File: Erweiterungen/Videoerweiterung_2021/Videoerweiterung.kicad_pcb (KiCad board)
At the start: 2 copper layers, 141.5 x 160 mm, 145 parts, among them X200 Bus, X201 ~CS2, X202 XTAL, X203 select, X204 ~KEY, X205 BUSY, X206 POWER, X300 8k RAM-Modul, X301 8k RAM-Modul, X302 8k RAM-Modul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

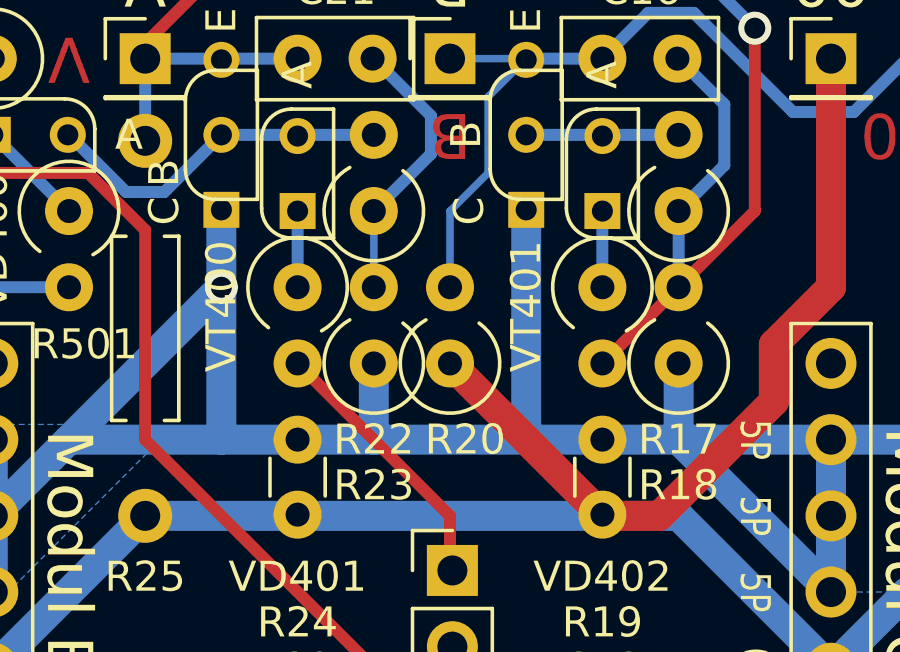
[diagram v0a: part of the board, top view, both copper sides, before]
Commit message: R20 gedreht
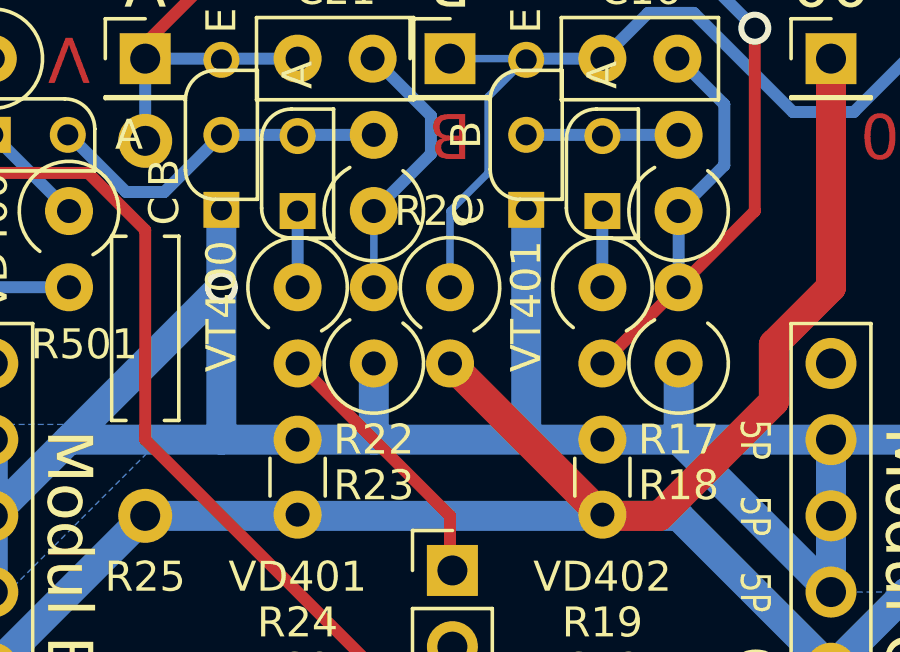
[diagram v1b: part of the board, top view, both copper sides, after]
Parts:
- D13: value UB8830 -> UB8860
- moved R20 2.54 mm to (121.9, 61.0), turned to 270 degrees
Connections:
- R20 pad 1: GND -> B
- R20 pad 2: B -> GND

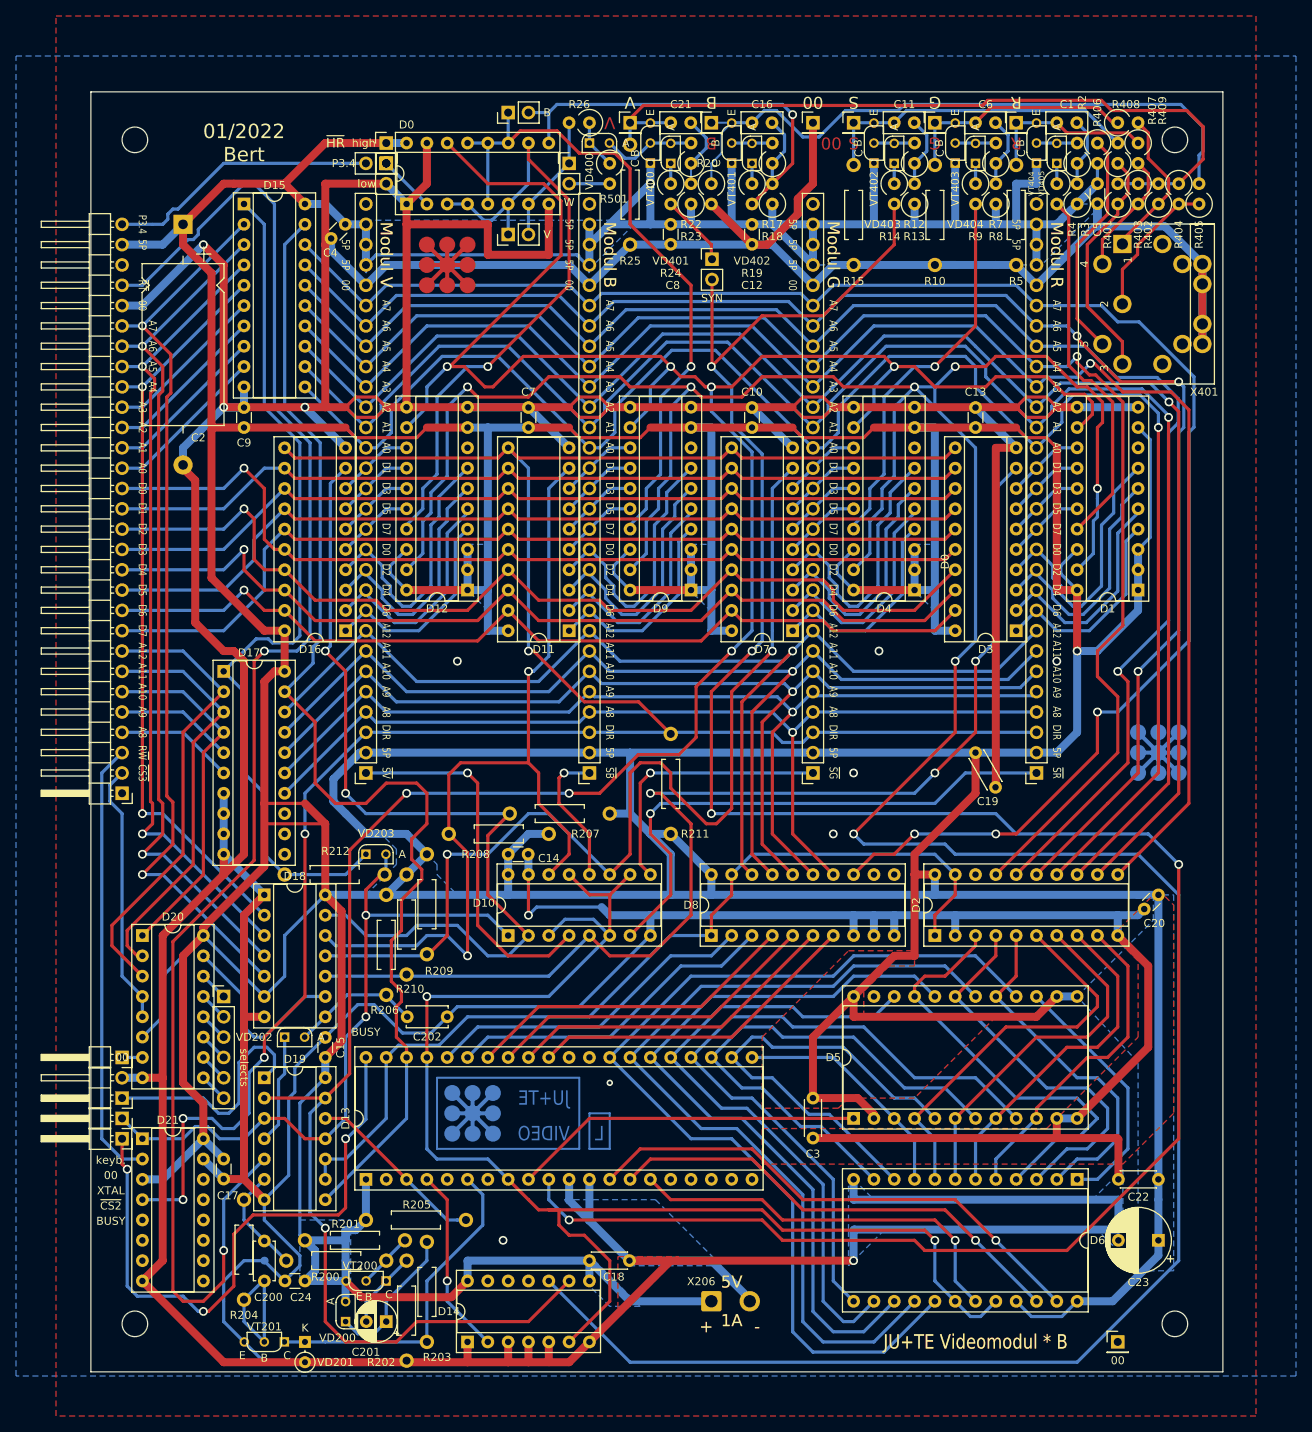
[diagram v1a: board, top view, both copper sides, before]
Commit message: PCB korrigiert
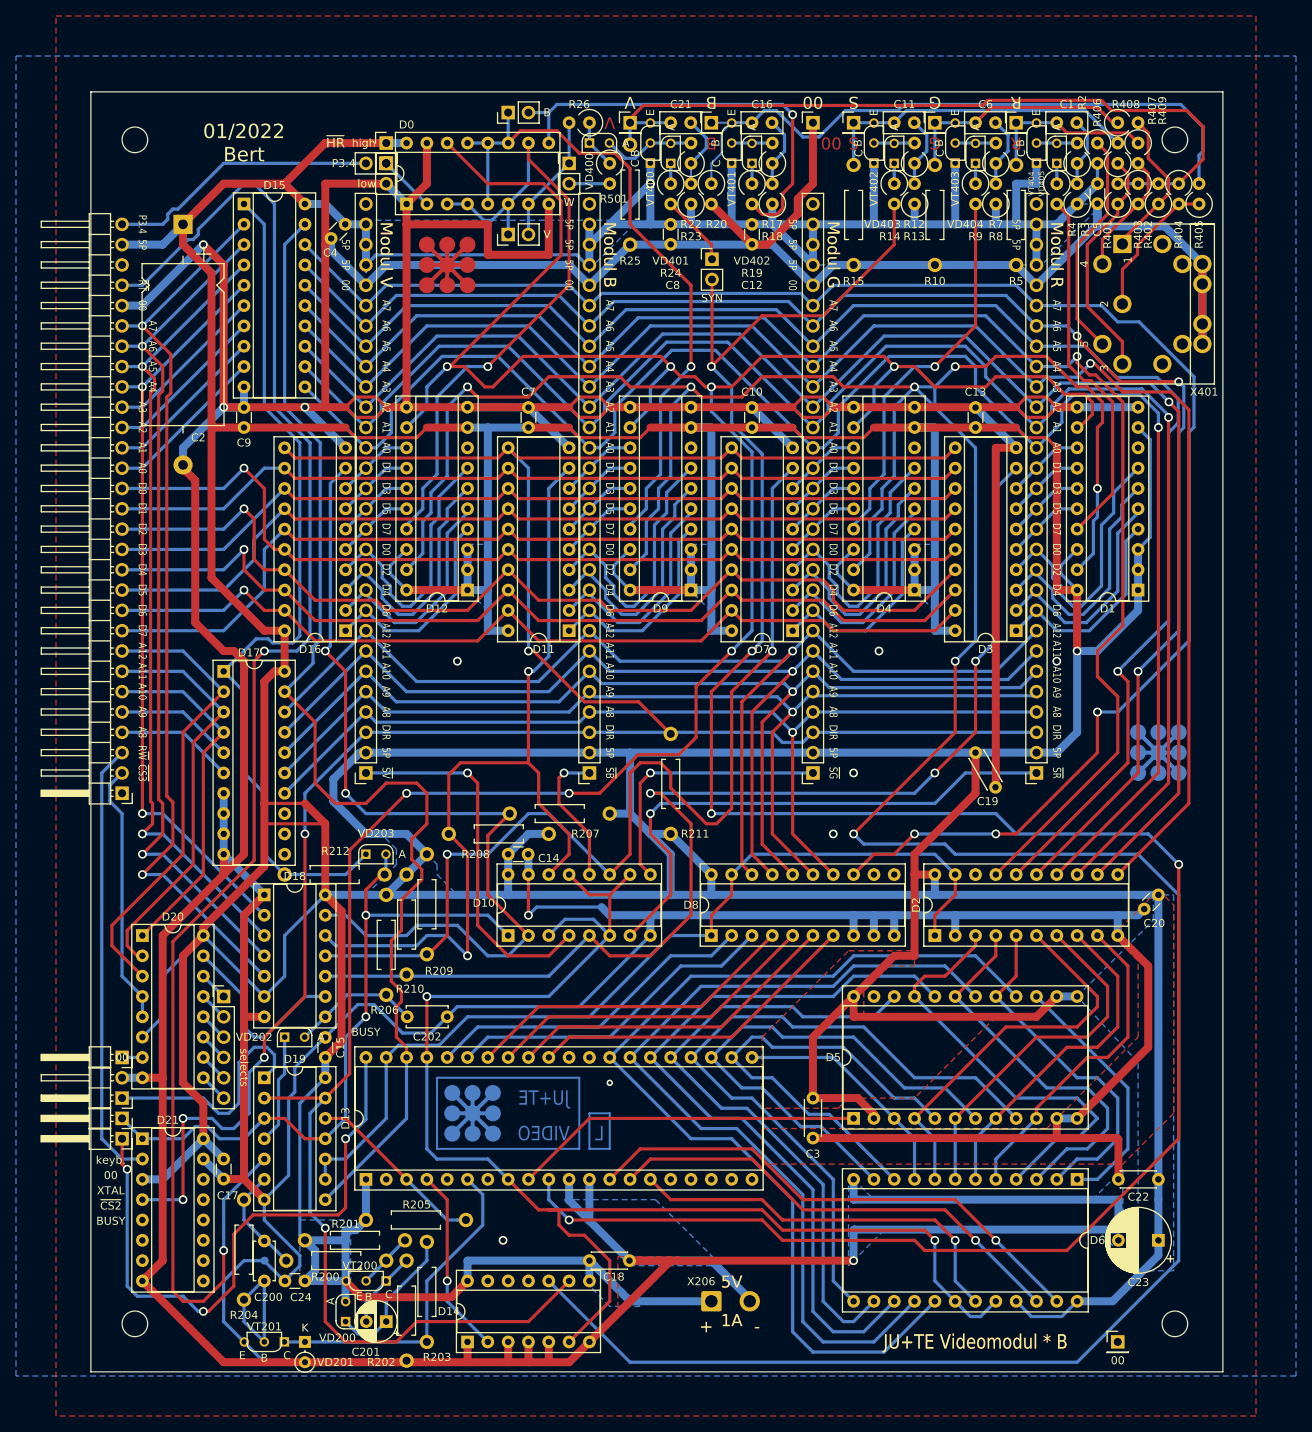
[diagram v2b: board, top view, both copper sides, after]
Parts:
- X201: value ~CS2 -> ~{CS2}
- X204: value ~KEY -> ~{KEY}
- moved ? 102.5 mm to (-1.27, -15.2)
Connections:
- net /Scart-Ausgang/~AV~RGB renamed /Scart-Ausgang/~{AV}RGB
- net /Videoausgabe/~HR renamed /Videoausgabe/~{HR}
- net /Videoprozessor/~VAS renamed /Videoprozessor/~{VAS}
- net /Videoprozessor/~VDS renamed /Videoprozessor/~{VDS}
- net /Videoprozessor/~VRT renamed /Videoprozessor/~{VRT}
- net R~W renamed R~{W}
- net ~CS2 renamed ~{CS2}
- net ~CS2_delay renamed ~{CS2_delay}
- net ~CS3 renamed ~{CS3}
- net ~EB renamed ~{EB}
- net ~EG renamed ~{EG}
- net ~ER renamed ~{ER}
- net ~EV renamed ~{EV}
- net ~SB renamed ~{SB}
- net ~SG renamed ~{SG}
- net ~SR renamed ~{SR}
- net ~SV renamed ~{SV}
- net ~SYN renamed ~{SYN}
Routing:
- net /Videoausgabe/b: track 51.1 -> 54.7 mm
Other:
- net class Default removed
- net class normal removed
- net class power removed
- board text added: "R~{W}"
- board text added: "~{CS2}"
- board text added: "~{CS3}"
- board text added: "~{HR}"
- board text added: "~{RT}"
- board text added: "~{SB}"
- board text added: "~{SG}"
- board text added: "~{SR}"
- board text added: "~{SV}"
- board text removed: "R~W"
- board text removed: "~CS2"
- board text removed: "~CS3"
- board text removed: "~HR~"
- board text removed: "~RT"
- board text removed: "~SB~"
- board text removed: "~SG~"
- board text removed: "~SR~"
- board text removed: "~SV~"
